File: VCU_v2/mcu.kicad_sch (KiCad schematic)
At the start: 35 parts, among them J2 NUCLEO CONNECTOR LEFT, J3 NUCLEO CONNECTOR RIGHT, SW1 SW_Push, U5 STM32H723ZGT6, Y1 16 MHz, Y2 32.768 kHz

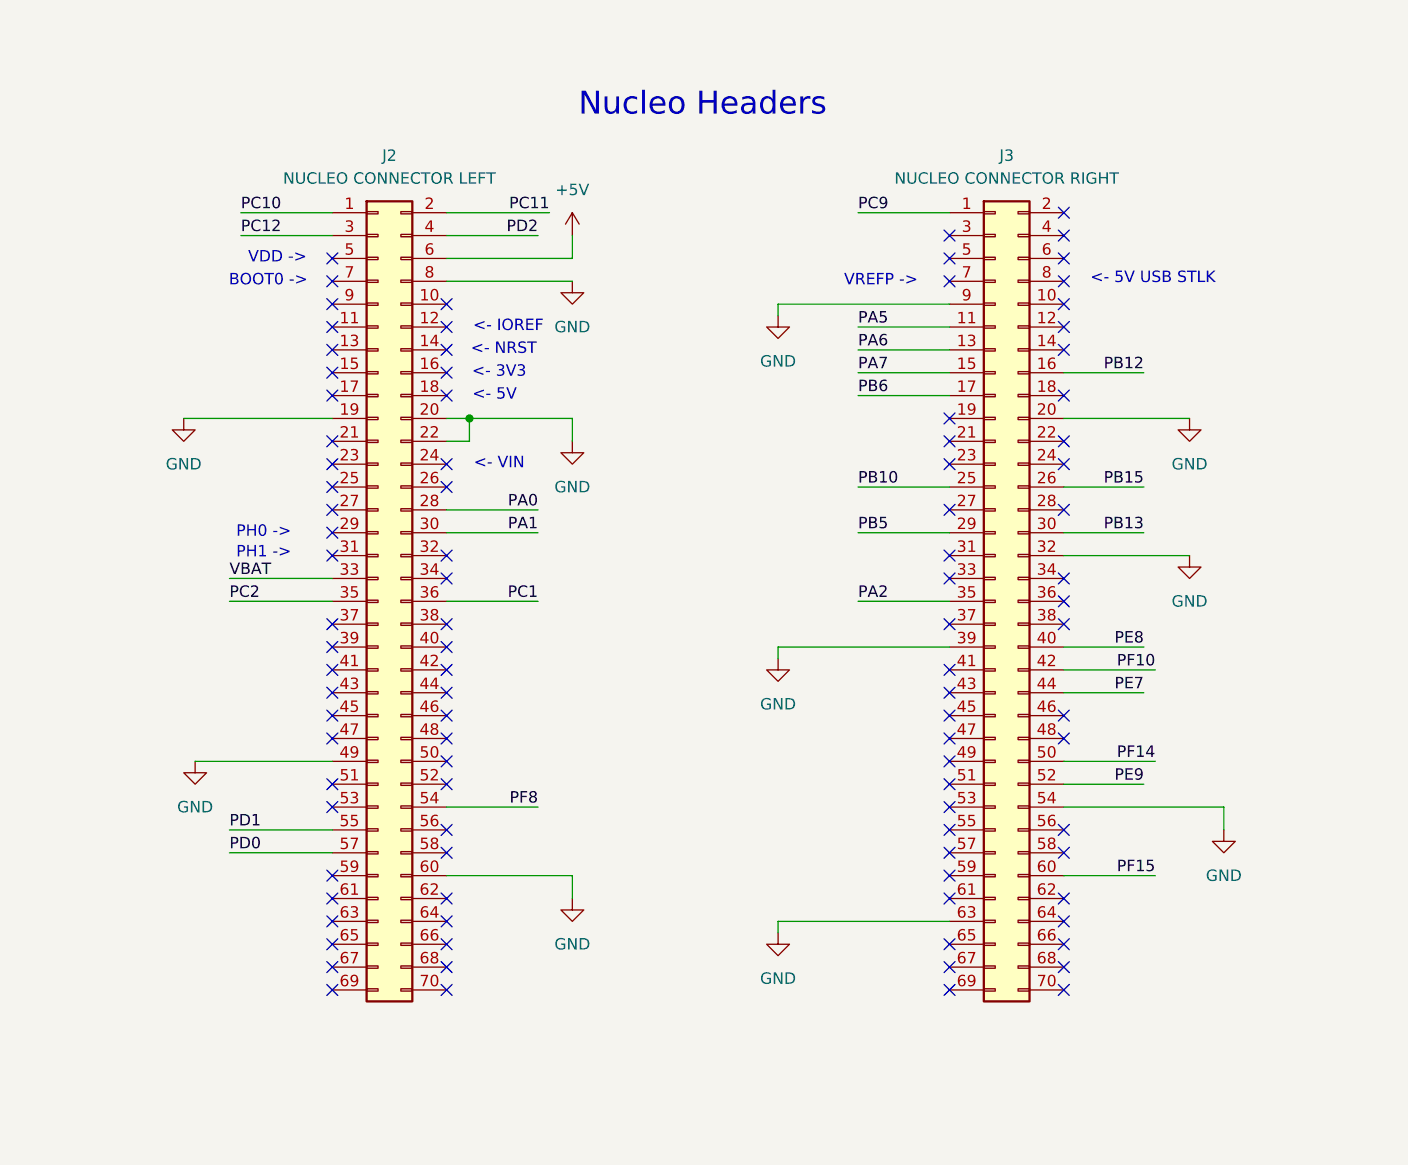
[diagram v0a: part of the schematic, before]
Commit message: slimed out nucleo in schematic
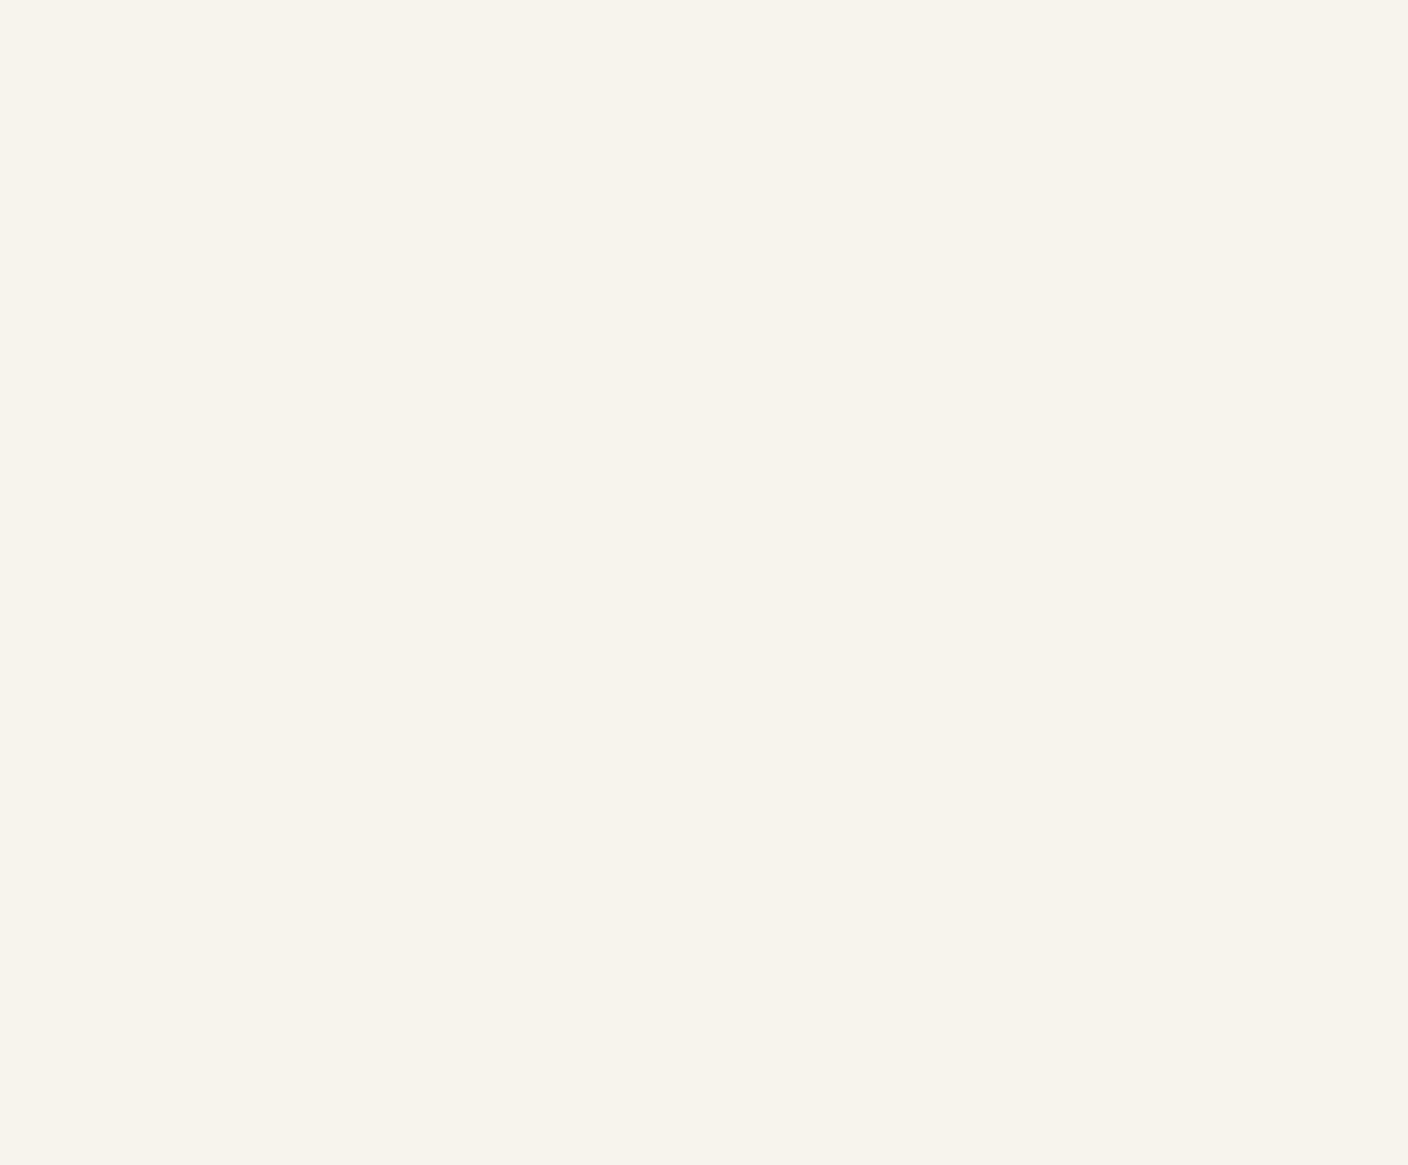
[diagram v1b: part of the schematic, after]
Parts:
- removed J2: NUCLEO CONNECTOR LEFT, Connector_PinHeader_2.54mm:PinHeader_2x35_P2.54mm_Vertical, symbol Connector_Generic:Conn_02x35_Odd_Even
- removed J3: NUCLEO CONNECTOR RIGHT, Connector_PinHeader_2.54mm:PinHeader_2x35_P2.54mm_Vertical, symbol Connector_Generic:Conn_02x35_Odd_Even
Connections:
- no-connect marks 99 -> 1
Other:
- note removed: "<- 3V3"
- note removed: "<- 5V"
- note removed: "<- 5V USB STLK"
- note removed: "<- IOREF"
- note removed: "<- NRST"
- note removed: "<- VIN"
- note removed: "BOOT0 ->"
- note removed: "Nucleo Headers"
- note removed: "PH0 ->"
- note removed: "PH1 ->"
- note removed: "VDD ->"
- note removed: "VREFP ->"

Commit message: vcu v2 schematics done
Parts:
- renumbered C18 to C12, C19 to C13, C20 to C14, C21 to C15, C22 to C16, C23 to C17, C24 to C18, C25 to C19, C26 to C20, C27 to C21, C28 to C22, C29 to C23, C30 to C24, C31 to C25, C32 to C26, C33 to C27, C34 to C28, C35 to C29, C36 to C30, C37 to C31, C38 to C32, C39 to C33, R9 to R5, R10 to R6, TP9 to TP16, TP7 to TP17, TP8 to TP18, U5 to U4

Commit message: placements friggin 80% friggin done shoutout epstein
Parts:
- renumbered C12 to C18, C13 to C19, C14 to C20, C15 to C21, C16 to C22, C17 to C23, C18 to C24, C19 to C25, C20 to C26, C21 to C27, C22 to C28, C23 to C29, C24 to C30, C25 to C31, C26 to C32, C27 to C33, C28 to C34, C29 to C35, C30 to C36, C31 to C37, C32 to C38, C33 to C39, R6 to R10, R5 to R9, TP17 to TP7, TP18 to TP8, TP16 to TP9, U4 to U5
